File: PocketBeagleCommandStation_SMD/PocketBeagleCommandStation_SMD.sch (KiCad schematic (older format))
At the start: 12 parts, among them J1 Console, J2 DCC Output to Tracks, P1 POCKETBEAGLE-P1, P2 POCKETBEAGLE-P2, P3 POCKETBEAGLE-Header, P4 POCKETBEAGLE-Header, T1 DCC Power In

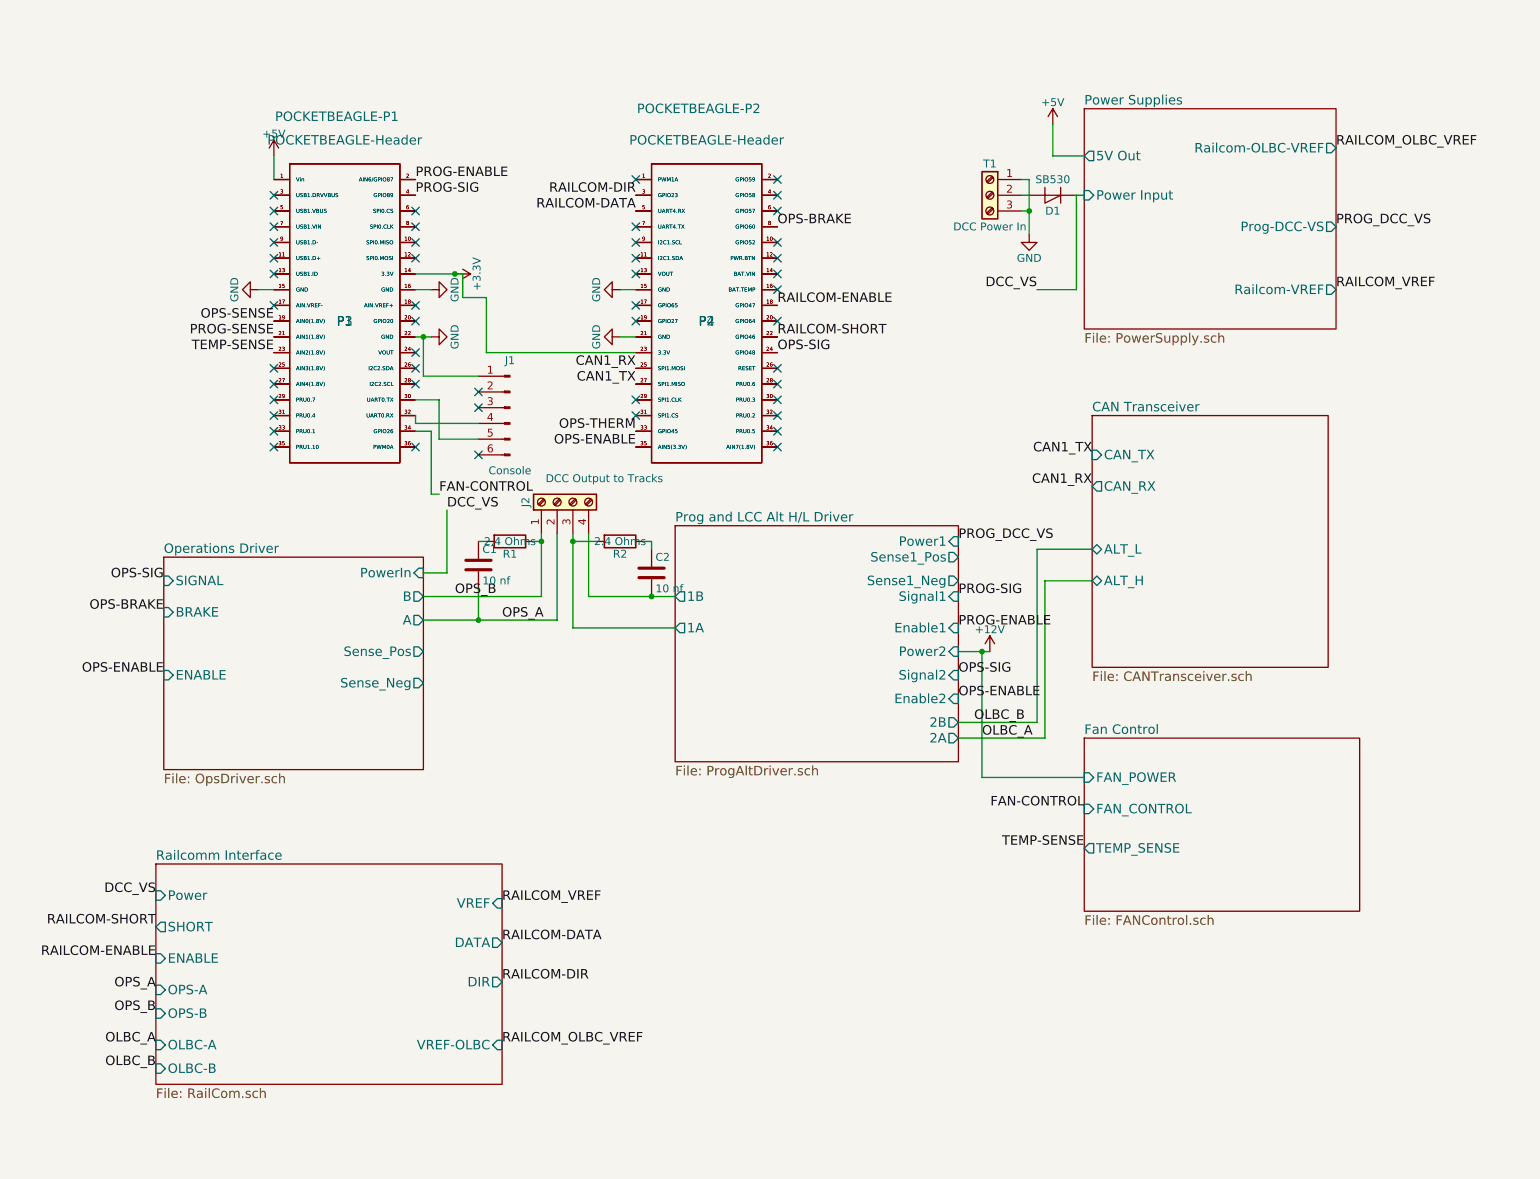
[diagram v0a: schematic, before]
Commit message: Continuing work on the SMD version of PocketBeagleCommandStation.
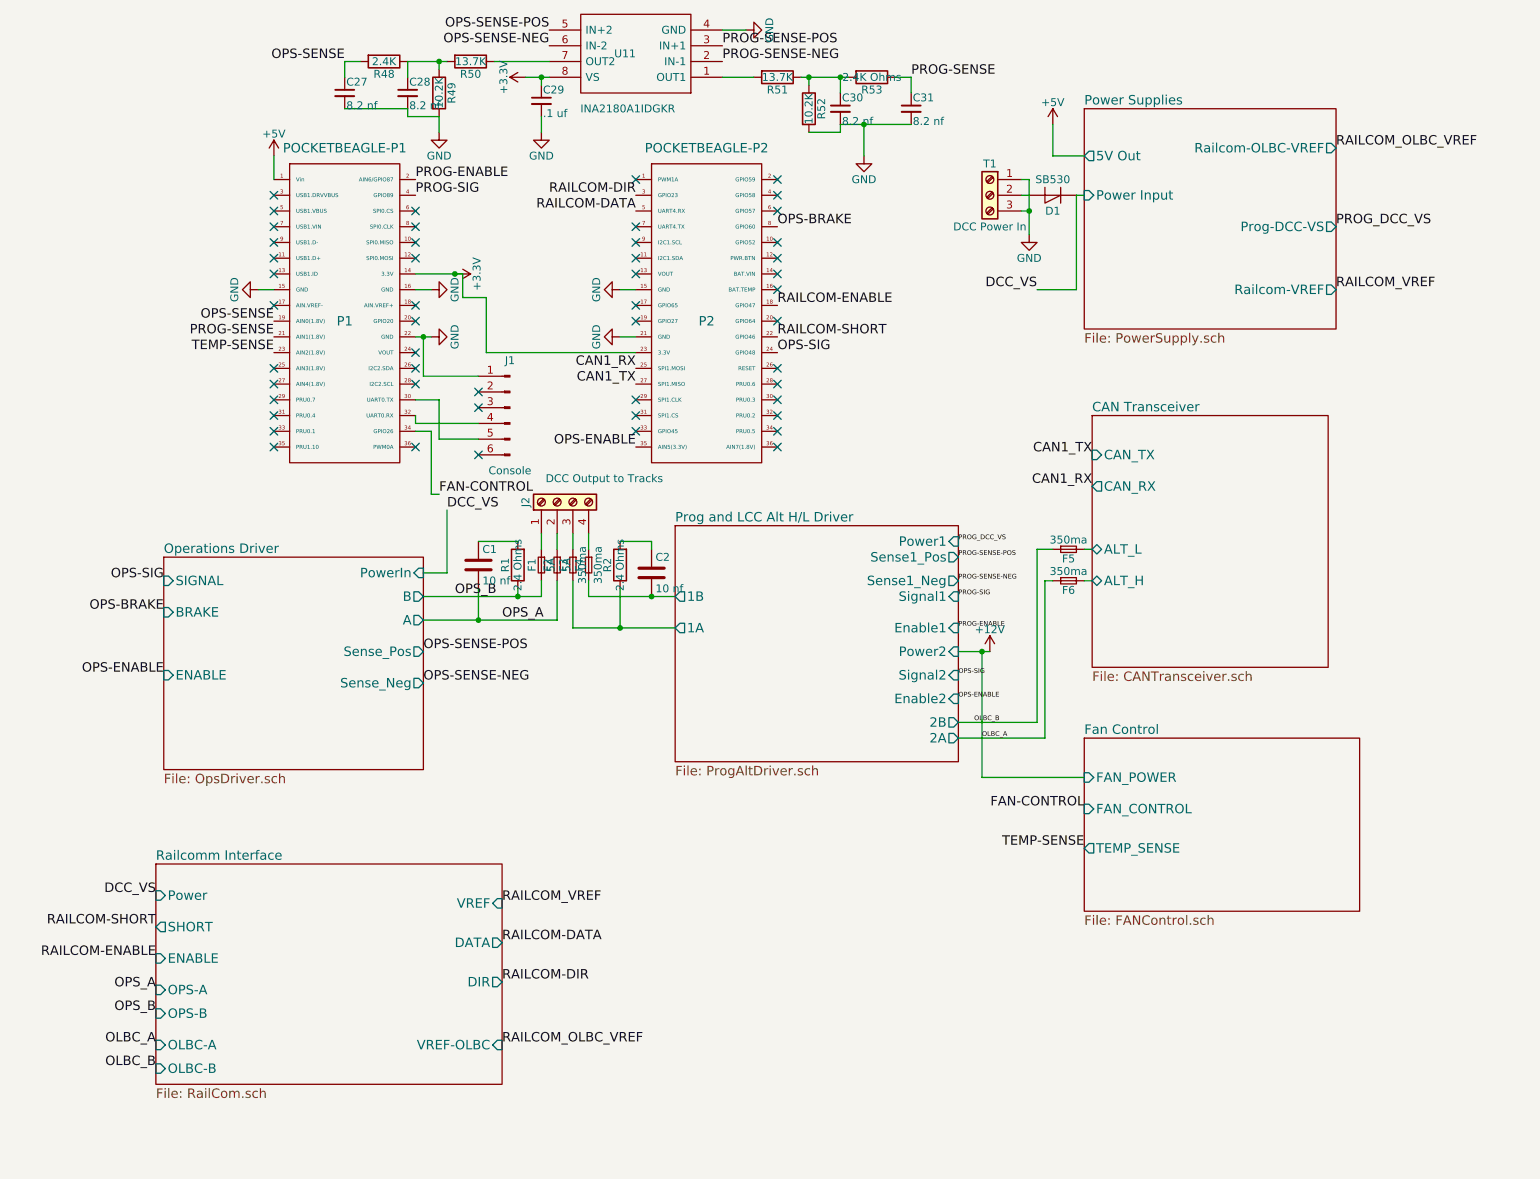
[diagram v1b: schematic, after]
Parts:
- removed P3: POCKETBEAGLE-Header, Socket_Strips:Socket_Strip_Straight_2x18_Pitch2.54mm, symbol POCKETBEAGLE-P1
- removed P4: POCKETBEAGLE-Header, Socket_Strips:Socket_Strip_Straight_2x18_Pitch2.54mm, symbol POCKETBEAGLE-P2
- added C27, C28, C30, C31: 8.2 nf, symbol C_Small
- added C29: .1 uf, symbol C_Small
- added F1, F2: 5A, symbol Fuse_Small
- added F3, F4, F5, F6: 350ma, symbol Fuse_Small
- added R48: 2.4K, symbol R
- added R49, R52: 10.2K, symbol R
- added R50, R51: 13.7K, symbol R
- added R53: 2.4K Ohms, symbol R
- added U11: INA2180A1IDGKR, SOP65P490X110-8N, symbol INA2180A1IDGKR
- P1, P2: footprint (none) -> Socket_Strips:Socket_Strip_Straight_2x18_Pitch2.54mm
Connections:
- net +12V: now also F6.1
- net +3V3: now also C29.1, U11.8 (VS)
- net GND: now also C27.2, C28.2, C29.2, C30.2, C31.2, R49.2, R52.2, U11.4 (GND)
- net OLBC_B: now also F5.1
- net OPS-SENSE: now also C27.1, R48.2
- net OPS_A: now also F2.2; no longer J2.2 (Pin_2)
- net OPS_B: now also F1.2; no longer J2.1 (Pin_1)
- net PROG-SENSE: now also C31.1, R53.1
- net Prog and LCC Alt H/L Driver/1A: now also R2.1, F3.2; no longer J2.3 (Pin_3), R2.2
- net Prog and LCC Alt H/L Driver/1B: now also F4.2; no longer J2.4 (Pin_4)
- net at C2.1: now also R2.2; no longer R2.1
- net OPS-THERM: no longer names the net of P2.33 (GPIO45)
- new net: F1.1, J2.1 (Pin_1)
- new net: F2.1, J2.2 (Pin_2)
- new net: F3.1, J2.3 (Pin_3)
- new net: F4.1, J2.4 (Pin_4)
- new net: R51.2, U11.1 (OUT1)
- new net: R50.1, U11.7 (OUT2)
- new net: C30.1, R51.1, R52.1, R53.2
- new net: C28.1, R48.1, R49.1, R50.2
- new net CAN Transceiver/ALT_H: F6.2
- new net CAN Transceiver/ALT_L: F5.2
- new net OPS-SENSE-NEG: U11.6 (IN-2)
- new net OPS-SENSE-POS: U11.5 (IN+2)
- new net PROG-SENSE-NEG: U11.2 (IN-1)
- new net PROG-SENSE-POS: U11.3 (IN+1)
- no-connect marks 49 -> 50
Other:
- moved on the sheet: R1, R2

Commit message: Continuing to work on PocketBeagleCommandStation_SMD.
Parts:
- added D11: OPS ActA, symbol LED_ALT
- added D12: OPS ActB, symbol LED_ALT
- added D13: PROG ActA, symbol LED_ALT
- added D14: PROG ActB, symbol LED_ALT
- added J7: USB_A, Connectors:USB_A, symbol USB_A
- added R54, R55, R56, R57: 3K, symbol R
- U11: footprint SOP65P490X110-8N -> INA2180A1IDGKR:SOP65P490X110-8N
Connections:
- net GND: now also P1.13 (USB1.ID), D11.1 (K), D12.1 (K), D13.1 (K), D14.1 (K), J7.4 (GND), J7.5 (Shield)
- net OPS_A: now also R54.1
- net OPS_B: now also R55.1
- net Prog and LCC Alt H/L Driver/1A: now also R56.1
- net Prog and LCC Alt H/L Driver/1B: now also R57.1
- net at P1.11 (USB1.D+): now also J7.3 (D+)
- net at P1.5 (USB1.VBUS): now also P1.7 (USB1.VIN), J7.1 (VBUS)
- net at P1.9 (USB1.D-): now also J7.2 (D-)
- new net: D11.2 (A), R54.2
- new net: D12.2 (A), R55.2
- new net: D13.2 (A), R56.2
- new net: D14.2 (A), R57.2
- no-connect marks 50 -> 45

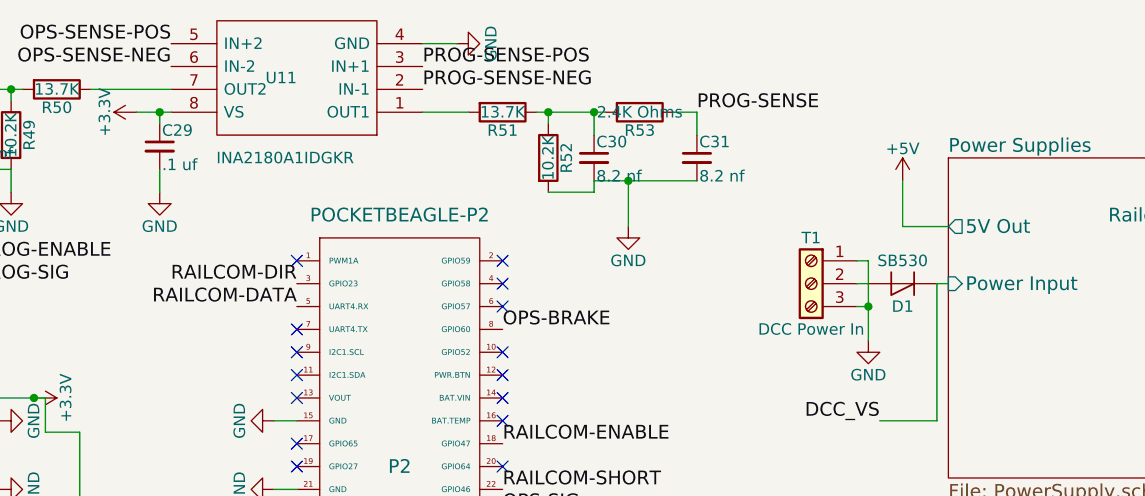
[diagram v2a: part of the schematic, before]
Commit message: Continuing with the PocketBeagle Command Station, SMD version.
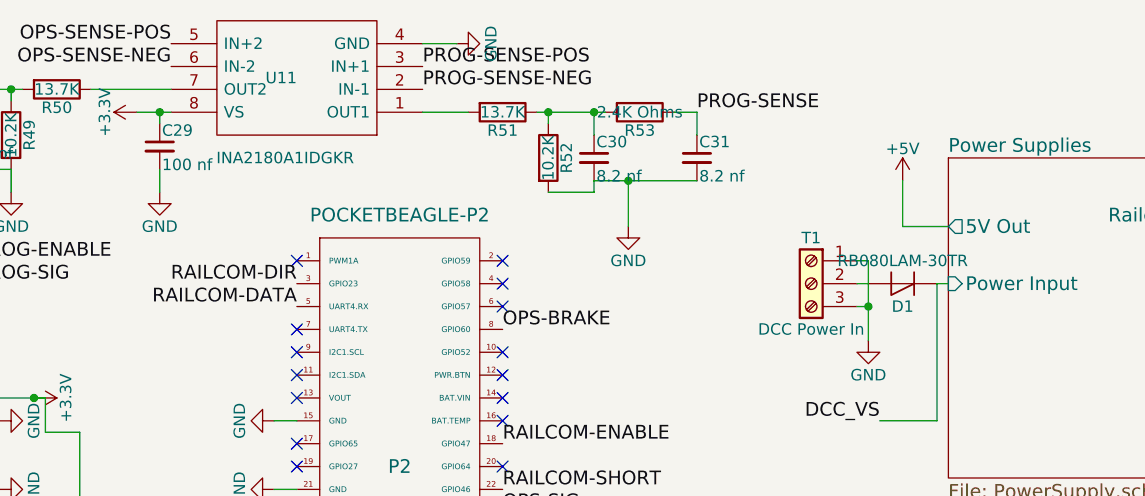
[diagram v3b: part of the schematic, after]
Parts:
- C1, C2: footprint Capacitors_THT:C_Rect_L4.0mm_W2.5mm_P2.50mm -> Capacitors_SMD:C_1206; Part Number 75-1C10Z5U103M100B -> 791-1206B103K500CT
- C27, C28, C30, C31: footprint (none) -> Capacitors_SMD:C_0603; Mouser Part Number (none) -> 791-0603B822K250CT
- C29: value .1 uf -> 100 nf; footprint (none) -> Capacitors_SMD:C_0603; Mouser Part Number (none) -> 603-CC603KPX7R9BB104
- D1: value SB530 -> RB080LAM-30TR; footprint Diodes_THT:D_DO-201AD_P12.70mm_Horizontal -> RB080LAM-30TR:PMDTM; Mouser Part Number (none) -> 755-RB080LAM-30TR; Part Number 625-SB530-E3 -> (none)
- D11, D13: footprint (none) -> LEDs:LED_0603; Mouser Part Number (none) -> 710-150060GS75000
- D12, D14: footprint (none) -> LEDs:LED_0603; Mouser Part Number (none) -> 710-150060RS75000
- F1, F2: footprint (none) -> MF-R500:MFR500; Mouser Part Number (none) -> 652-MFR500
- F3: footprint (none) -> 0ZCG0035AF2C:FUSC4632X70N; Mouser Part Number (none) -> 530-0ZCG0035AF2C
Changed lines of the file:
@@
 P 7350 1750
 F 0 "D1" H 7350 1850 50  0000 C CNN
-F 1 "SB530" H 7350 1650 50  0000 C CNN
-F 2 "Diodes_THT:D_DO-201AD_P12.70mm_Horizontal" H 7350 1750 50  0001 C CNN
+F 1 "RB080LAM-30TR" H 7350 1650 50  0000 C CNN
+F 2 "RB080LAM-30TR:PMDTM" H 7350 1750 50  0001 C CNN
 F 3 "" H 7350 1750 50  0001 C CNN
-F 4 "625-SB530-E3" H 7350 1750 60  0001 C CNN "Part Number"
+F 4 "755-RB080LAM-30TR" H 7350 1750 60  0001 C CNN "Mouser Part Number"
 	1    7350 1750
 	-1   0    0    1
@@
 F 0 "C1" H 3725 4200 50  0000 L CNN
 F 1 "10 nf" H 3725 4000 50  0000 L CNN
-F 2 "Capacitors_THT:C_Rect_L4.0mm_W2.5mm_P2.50mm" H 3738 3950 50  0001 C CNN
+F 2 "Capacitors_SMD:C_1206" H 3738 3950 50  0001 C CNN
 F 3 "" H 3700 4100 50  0001 C CNN
-F 4 "75-1C10Z5U103M100B" H 3700 4100 60  0001 C CNN "Part Number"
+F 4 "791-1206B103K500CT" H 3700 4100 60  0001 C CNN "Part Number"
 	1    3700 4100
 	1    0    0    -1
@@
 F 0 "C2" H 4825 4250 50  0000 L CNN
 F 1 "10 nf" H 4825 4050 50  0000 L CNN
-F 2 "Capacitors_THT:C_Rect_L4.0mm_W2.5mm_P2.50mm" H 4838 4000 50  0001 C CNN
+F 2 "Capacitors_SMD:C_1206" H 4838 4000 50  0001 C CNN
 F 3 "" H 4800 4150 50  0001 C CNN
-F 4 "75-1C10Z5U103M100B" H 4800 4150 60  0001 C CNN "Part Number"
+F 4 "791-1206B103K500CT" H 4800 4150 60  0001 C CNN "Part Number"
 	1    4800 4150
 	1    0    0    -1
@@
 F 0 "F1" H 4100 4040 50  0000 C CNN
 F 1 "5A" H 4100 4160 50  0000 C CNN
-F 2 "" H 4100 4100 50  0001 C CNN
+F 2 "MF-R500:MFR500" H 4100 4100 50  0001 C CNN
 F 3 "" H 4100 4100 50  0001 C CNN
+F 4 "652-MFR500 " H 4100 4100 60  0001 C CNN "Mouser Part Number"
 	1    4100 4100
 	0    1    1    0
@@
 F 0 "F2" H 4200 4040 50  0000 C CNN
 F 1 "5A" H 4200 4160 50  0000 C CNN
-F 2 "" H 4200 4100 50  0001 C CNN
+F 2 "MF-R500:MFR500" H 4200 4100 50  0001 C CNN
 F 3 "" H 4200 4100 50  0001 C CNN
+F 4 "652-MFR500 " H 4200 4100 60  0001 C CNN "Mouser Part Number"
 	1    4200 4100
 	0    1    1    0
@@
 F 0 "F3" H 4300 4040 50  0000 C CNN
 F 1 "350ma" H 4300 4160 50  0000 C CNN
-F 2 "" H 4300 4100 50  0001 C CNN
+F 2 "0ZCG0035AF2C:FUSC4632X70N" H 4300 4100 50  0001 C CNN
 F 3 "" H 4300 4100 50  0001 C CNN
+F 4 "530-0ZCG0035AF2C " H 4300 4100 60  0001 C CNN "Mouser Part Number"
 	1    4300 4100
 	0    1    1    0
@@
 F 0 "C30" H 6010 1270 50  0000 L CNN
 F 1 "8.2 nf" H 6010 1120 50  0000 L CNN
-F 2 "" H 6000 1200 50  0001 C CNN
+F 2 "Capacitors_SMD:C_0603" H 6000 1200 50  0001 C CNN
 F 3 "" H 6000 1200 50  0001 C CNN
+F 4 "791-0603B822K250CT" H 6000 1200 60  0001 C CNN "Mouser Part Number"
 	1    6000 1200
 	1    0    0    -1
@@
 F 0 "C31" H 6460 1270 50  0000 L CNN
 F 1 "8.2 nf" H 6460 1120 50  0000 L CNN
-F 2 "" H 6450 1200 50  0001 C CNN
+F 2 "Capacitors_SMD:C_0603" H 6450 1200 50  0001 C CNN
 F 3 "" H 6450 1200 50  0001 C CNN
+F 4 "791-0603B822K250CT" H 6450 1200 60  0001 C CNN "Mouser Part Number"
 	1    6450 1200
 	1    0    0    -1
@@
 F 0 "C28" H 3260 1170 50  0000 L CNN
 F 1 "8.2 nf" H 3260 1020 50  0000 L CNN
-F 2 "" H 3250 1100 50  0001 C CNN
+F 2 "Capacitors_SMD:C_0603" H 3250 1100 50  0001 C CNN
 F 3 "" H 3250 1100 50  0001 C CNN
+F 4 "791-0603B822K250CT" H 3250 1100 60  0001 C CNN "Mouser Part Number"
 	1    3250 1100
 	1    0    0    -1
@@
 F 0 "C27" H 2860 1170 50  0000 L CNN
 F 1 "8.2 nf" H 2860 1020 50  0000 L CNN
-F 2 "" H 2850 1100 50  0001 C CNN
+F 2 "Capacitors_SMD:C_0603" H 2850 1100 50  0001 C CNN
 F 3 "" H 2850 1100 50  0001 C CNN
+F 4 "791-0603B822K250CT" H 2850 1100 60  0001 C CNN "Mouser Part Number"
 	1    2850 1100
 	1    0    0    -1
@@
 P 4100 1150
 F 0 "C29" H 4110 1220 50  0000 L CNN
-F 1 ".1 uf" H 4110 1070 50  0000 L CNN
-F 2 "" H 4100 1150 50  0001 C CNN
+F 1 "100 nf" H 4110 1070 50  0000 L CNN
+F 2 "Capacitors_SMD:C_0603" H 4100 1150 50  0001 C CNN
 F 3 "" H 4100 1150 50  0001 C CNN
+F 4 "603-CC603KPX7R9BB104" H 4100 1150 60  0001 C CNN "Mouser Part Number"
 	1    4100 1150
 	1    0    0    -1
@@
 F 0 "D11" H 3700 5500 50  0000 C CNN
 F 1 "OPS ActA" H 3700 5300 50  0000 C CNN
-F 2 "" H 3700 5400 50  0001 C CNN
+F 2 "LEDs:LED_0603" H 3700 5400 50  0001 C CNN
 F 3 "" H 3700 5400 50  0001 C CNN
+F 4 "710-150060GS75000" H 3700 5400 60  0001 C CNN "Mouser Part Number"
 	1    3700 5400
 	0    -1   -1   0
@@
 F 0 "D12" H 3950 5500 50  0000 C CNN
 F 1 "OPS ActB" H 3950 5300 50  0000 C CNN
-F 2 "" H 3950 5400 50  0001 C CNN
+F 2 "LEDs:LED_0603" H 3950 5400 50  0001 C CNN
 F 3 "" H 3950 5400 50  0001 C CNN
+F 4 "710-150060RS75000 " H 3950 5400 60  0001 C CNN "Mouser Part Number"
 	1    3950 5400
 	0    -1   -1   0
@@
 F 0 "D13" H 4450 5500 50  0000 C CNN
 F 1 "PROG ActA" H 4450 5300 50  0000 C CNN
-F 2 "" H 4450 5400 50  0001 C CNN
+F 2 "LEDs:LED_0603" H 4450 5400 50  0001 C CNN
 F 3 "" H 4450 5400 50  0001 C CNN
+F 4 "710-150060GS75000" H 4450 5400 60  0001 C CNN "Mouser Part Number"
 	1    4450 5400
 	0    -1   -1   0
@@
 F 0 "D14" H 4700 5500 50  0000 C CNN
 F 1 "PROG ActB" H 4700 5300 50  0000 C CNN
-F 2 "" H 4700 5400 50  0001 C CNN
+F 2 "LEDs:LED_0603" H 4700 5400 50  0001 C CNN
 F 3 "" H 4700 5400 50  0001 C CNN
+F 4 "710-150060RS75000 " H 4700 5400 60  0001 C CNN "Mouser Part Number"
 	1    4700 5400
 	0    -1   -1   0

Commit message: Continuing working on PocketBeagleCommandStation_SMD.
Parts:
- F4, F5, F6: footprint (none) -> 0ZCG0035AF2C:FUSC4632X70N; Mouser Part Number (none) -> 530-0ZCG0035AF2C
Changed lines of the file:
@@
 LIBS:INA2180A1IDGKR
 LIBS:lm2574n-5
+LIBS:mechanical
+LIBS:references
+LIBS:motors
+LIBS:graphic_symbols
+LIBS:motor_drivers
+LIBS:irf7351pbf
 LIBS:PocketBeagleCommandStation_SMD-cache
 EELAYER 25 0
@@
 F 0 "F4" H 4400 4040 50  0000 C CNN
 F 1 "350ma" H 4400 4160 50  0000 C CNN
-F 2 "" H 4400 4100 50  0001 C CNN
+F 2 "0ZCG0035AF2C:FUSC4632X70N" H 4400 4100 50  0001 C CNN
 F 3 "" H 4400 4100 50  0001 C CNN
+F 4 "530-0ZCG0035AF2C " H 4400 4100 60  0001 C CNN "Mouser Part Number"
 	1    4400 4100
 	0    1    1    0
@@
 F 0 "F5" H 7450 3940 50  0000 C CNN
 F 1 "350ma" H 7450 4060 50  0000 C CNN
-F 2 "" H 7450 4000 50  0001 C CNN
+F 2 "0ZCG0035AF2C:FUSC4632X70N" H 7450 4000 50  0001 C CNN
 F 3 "" H 7450 4000 50  0001 C CNN
+F 4 "530-0ZCG0035AF2C" H 7450 4000 60  0001 C CNN "Mouser Part Number"
 	1    7450 4000
 	1    0    0    -1
@@
 F 0 "F6" H 7450 4140 50  0000 C CNN
 F 1 "350ma" H 7450 4260 50  0000 C CNN
-F 2 "" H 7450 4200 50  0001 C CNN
-F 3 "" H 7450 4200 50  0001 C CNN
+F 2 "0ZCG0035AF2C:FUSC4632X70N" H 7450 4200 50  0001 C CNN
+F 3 "530-0ZCG0035AF2C" H 7450 4200 50  0001 C CNN
+F 4 "530-0ZCG0035AF2C" H 7450 4200 60  0001 C CNN "Mouser Part Number"
 	1    7450 4200
 	1    0    0    -1
